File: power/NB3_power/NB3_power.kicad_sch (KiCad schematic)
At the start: 33 parts, among them J1 Barrel_Jack_PJ-036AH-SMT-TR, J2 Connector_S4B-PH-SM4-TB(LF)(S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, SW1 SW_SPDT, U1 Voltage_Regulator_AP64501

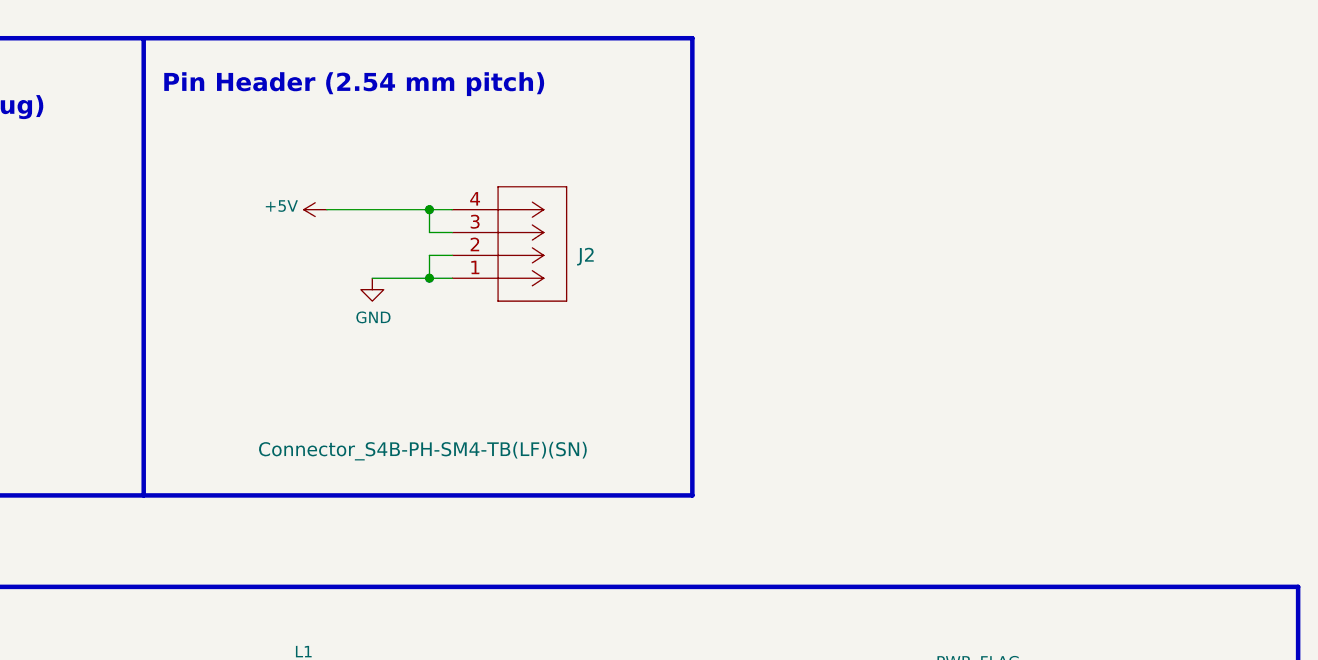
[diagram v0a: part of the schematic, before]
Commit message: Update PCBs (body, ear, mouth, and power)
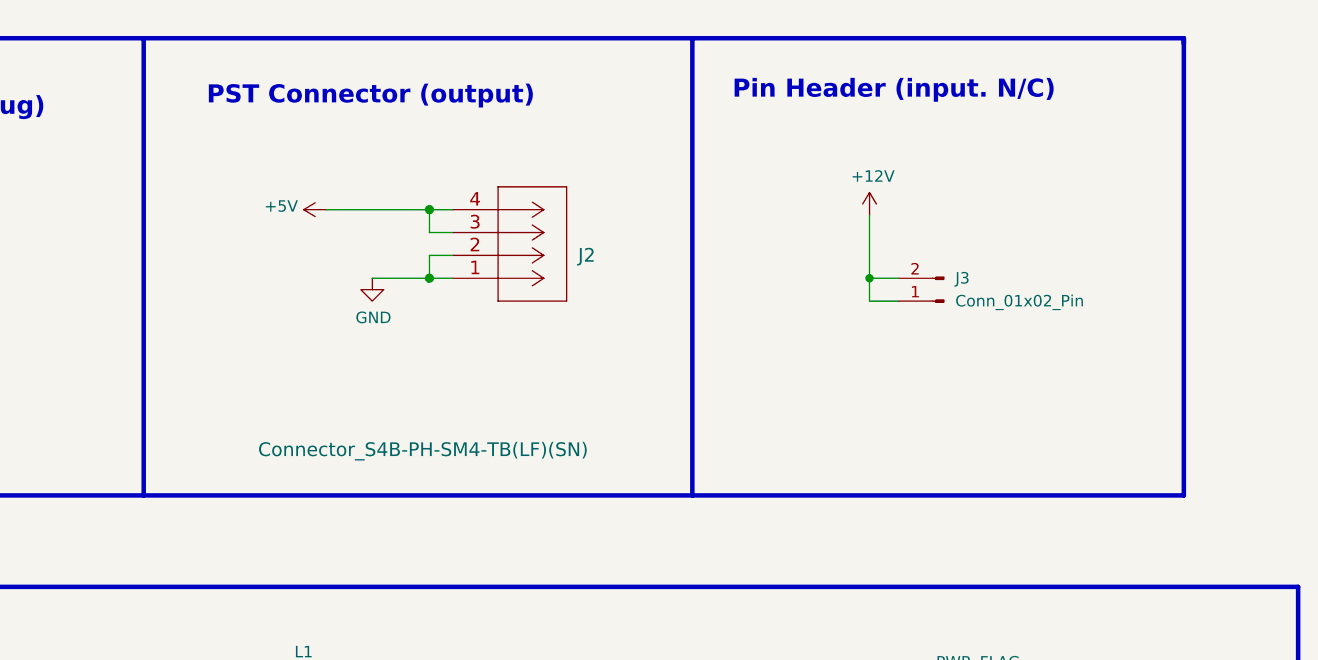
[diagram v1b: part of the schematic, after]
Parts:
- added J3: Conn_01x02_Pin, Connector_PinHeader_2.54mm:PinHeader_1x02_P2.54mm_Horizontal, symbol Connector:Conn_01x02_Pin
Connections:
- net +12V: now also J3.1 (Pin_1), J3.2 (Pin_2)
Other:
- note added: "PST Connector (output)"
- note added: "Pin Header (input. N/C)"
- note removed: "Pin Header (2.54 mm pitch)"
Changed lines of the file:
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@@
   (title_block
     (title "NB3 Power Board")
-    (date "2023-08-03")
-    (rev "0.0.4")
+    (date "2023-11-29")
+    (rev "0.0.5")
     (company "Voight-Kampff")
     (comment 1 "NoBlackBoxes: NB3 power source")
@@
   (junction (at 156.21 139.7) (diameter 1.016) (color 0 0 0 0)
   )
+  (junction (at 235.585 57.15) (diameter 0) (color 0 0 0 0)
+  )
   (junction (at 181.61 110.49) (diameter 1.016) (color 0 0 0 0)
   )
@@
     (stroke (width 0) (type solid))
   )
+  (wire (pts (xy 238.76 59.69) (xy 235.585 59.69))
+    (stroke (width 0) (type default))
+  )
   (wire (pts (xy 171.45 139.7) (xy 181.61 139.7))
     (stroke (width 0) (type solid))
@@
     (stroke (width 0) (type solid))
   )
+  (wire (pts (xy 235.585 57.15) (xy 238.76 57.15))
+    (stroke (width 0) (type default))
+  )
   (wire (pts (xy 189.23 57.15) (xy 186.69 57.15))
     (stroke (width 0) (type solid))
@@
     (stroke (width 0) (type solid))
   )
+  (polyline (pts (xy 270.51 30.48) (xy 270.51 81.28))
+    (stroke (width 0.5) (type solid))
+  )
   (wire (pts (xy 73.66 118.11) (xy 83.82 118.11))
     (stroke (width 0) (type solid))
@@
     (stroke (width 0) (type solid))
   )
+  (polyline (pts (xy 270.51 30.48) (xy 270.51 31.115))
+    (stroke (width 0.5) (type solid))
+  )
   (wire (pts (xy 226.06 111.76) (xy 226.06 119.38))
     (stroke (width 0) (type solid))
@@
   (wire (pts (xy 181.61 123.19) (xy 181.61 130.81))
     (stroke (width 0) (type solid))
+  )
+  (wire (pts (xy 235.585 59.69) (xy 235.585 57.15))
+    (stroke (width 0) (type default))
   )
   (polyline (pts (xy 13.97 91.44) (xy 13.97 147.32))
@@
     (stroke (width 0.5) (type solid))
   )
+  (wire (pts (xy 235.585 50.165) (xy 235.585 57.15))
+    (stroke (width 0) (type default))
+  )
   (wire (pts (xy 203.2 111.76) (xy 203.2 119.38))
     (stroke (width 0) (type solid))
@@
     (stroke (width 0) (type solid))
   )
+  (polyline (pts (xy 215.9 30.48) (xy 270.51 30.48))
+    (stroke (width 0.5) (type solid))
+  )
   (wire (pts (xy 161.925 120.65) (xy 171.45 120.65))
     (stroke (width 0) (type solid))
@@
     (stroke (width 0) (type solid))
   )
+  (polyline (pts (xy 215.9 81.28) (xy 270.51 81.28))
+    (stroke (width 0.5) (type solid))
+  )
   (wire (pts (xy 123.19 64.77) (xy 123.19 67.31))
     (stroke (width 0) (type solid))
@@
   (wire (pts (xy 119.38 135.89) (xy 119.38 139.7))
     (stroke (width 0) (type solid))
+  )
+  (text "Pin Header (input. N/C)" (at 220.345 37.465 0)
+    (effects (font (size 2 2) (thickness 0.4) bold) (justify left bottom))
   )
   (text "Mounting Holes" (at 73.152 165.1 0)
     (effects (font (size 2 2) (thickness 0.4) bold) (justify left bottom))
   )
-  (text "Pin Header (2.54 mm pitch)" (at 156.972 36.83 0)
+  (text "PST Connector (output)" (at 161.925 38.1 0)
     (effects (font (size 2 2) (thickness 0.4) bold) (justify left bottom))
   )
@@
         (path "/865a6659-88ab-4157-bbc8-8818e83bf79d"
           (reference "#PWR06") (unit 1)
+        )
+      )
+    )
+  )
+  (symbol (lib_id "Connector:Conn_01x02_Pin") (at 243.84 59.69 180) (unit 1)
+    (in_bom yes) (on_board yes) (dnp no) (fields_autoplaced)
+    (property "Reference" "J3" (at 245.11 57.15 0)
+      (effects (font (size 1.27 1.27)) (justify right))
+    )
+    (property "Value" "Conn_01x02_Pin" (at 245.11 59.69 0)
+      (effects (font (size 1.27 1.27)) (justify right))
+    )
+    (property "Footprint" "Connector_PinHeader_2.54mm:PinHeader_1x02_P2.54mm_Horizontal" (at 243.84 59.69 0)
+      (effects (font (size 1.27 1.27)) hide)
+    )
+    (property "Datasheet" "~" (at 243.84 59.69 0)
+      (effects (font (size 1.27 1.27)) hide)
+    )
+    (pin "1")
+    (pin "2")
+    (instances
+      (project "NB3_power"
+        (path "/865a6659-88ab-4157-bbc8-8818e83bf79d"
+          (reference "J3") (unit 1)
         )
       )
@@
         )
       )
+    )
+  )
+  (symbol (lib_id "power:+12V") (at 235.585 50.165 0) (unit 1)
+    (in_bom yes) (on_board yes) (dnp no)
+    (property "Reference" "#PWR09" (at 235.585 53.975 0)
+      (effects (font (size 1.27 1.27)) hide)
+    )
+    (property "Value" "+12V" (at 235.9533 45.8406 0)
+      (effects (font (size 1.27 1.27)))
+    )
+    (property "Footprint" "" (at 235.585 50.165 0)
+      (effects (font (size 1.27 1.27)) hide)
+    )
+    (property "Datasheet" "" (at 235.585 50.165 0)
+      (effects (font (size 1.27 1.27)) hide)
+    )
+    (pin "1")
+    (instances
+      (project "NB3_power"
+        (path "/865a6659-88ab-4157-bbc8-8818e83bf79d"
+          (reference "#PWR09") (unit 1)
+        )
+      )
